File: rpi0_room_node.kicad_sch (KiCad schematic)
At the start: 38 parts, among them J1 Raspberry Pi, J2 Conn_01x03, J3 Conn_01x03, J4 Conn_01x03, Q1 PDTC123Y, U1 AP2210K-3.3, U2 TSOP382xx, U3 RFM69HCW

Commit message: Add ADS1015 ADC
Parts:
- removed AE1: SMA, Connector_Coaxial:SMA_Amphenol_132289_EdgeMount, symbol Device:Antenna_Shield
- removed AE2: U.FL, Connector_Coaxial:U.FL_Hirose_U.FL-R-SMT-1_Vertical, symbol Device:Antenna_Shield
- removed C4: 10u, Capacitor_SMD:C_0805_2012Metric_Pad1.15x1.40mm_HandSolder, symbol Device:C
- removed D1: ASMB-MTB0-0A3A2, LED_SMD:LED_Avago_PLCC4_3.2x2.8mm_CW, symbol LED:ASMB-MTB0-0A3A2
- removed D2: CQY99, LED_THT:LED_D5.0mm_IRGrey, symbol LED:CQY99
- removed D3, D4, D5: LED, LED_SMD:LED_0805_2012Metric_Castellated, symbol Device:LED
- removed J2, J4: Conn_01x03, Connector_PinHeader_2.54mm:PinHeader_1x03_P2.54mm_Vertical, symbol Connector_Generic:Conn_01x03
- removed Q1: PDTC123Y, Package_TO_SOT_SMD:SC-59_Handsoldering, symbol Transistor_BJT:DTA123E
- removed TP5, TP6, TP7: TestPoint, TestPoint:TestPoint_THTPad_1.0x1.0mm_Drill0.5mm, symbol Connector:TestPoint
- removed U1: AP2210K-3.3, Package_TO_SOT_SMD:SOT-23-5, symbol Regulator_Linear:AP2204K-3.3
- removed U2: TSOP382xx, OptoDevice:Vishay_MINICAST-3Pin, symbol Interface_Optical:TSOP382xx
- removed U3: RFM69HCW, RF_Module:HOPERF_RFM69HW, symbol RF_AM_FM:RFM69HCW
- added U1: ADS1015IDGS, Package_SO:TSSOP-10_3x3mm_P0.5mm, symbol Analog_ADC:ADS1015IDGS
- added U2, U3: DS18B20, Connector_PinHeader_2.54mm:PinHeader_1x03_P2.54mm_Vertical, symbol Sensor_Temperature:DS18B20
- C1: value 1u -> 100n; footprint Capacitor_SMD:C_0805_2012Metric_Pad1.15x1.40mm_HandSolder -> Capacitor_SMD:C_0402_1005Metric_Pad0.74x0.62mm_HandSolder
- C2: value 10u -> 100n; footprint Capacitor_SMD:C_0805_2012Metric_Pad1.15x1.40mm_HandSolder -> Capacitor_SMD:C_0402_1005Metric_Pad0.74x0.62mm_HandSolder
- C3: footprint Capacitor_SMD:C_0805_2012Metric_Pad1.15x1.40mm_HandSolder -> Capacitor_SMD:C_0805_2012Metric_Pad1.18x1.45mm_HandSolder
- R1: footprint Resistor_SMD:R_0805_2012Metric_Pad1.15x1.40mm_HandSolder -> Resistor_SMD:R_0402_1005Metric_Pad0.72x0.64mm_HandSolder
- R2: value 70 -> R; footprint Resistor_SMD:R_0805_2012Metric_Pad1.15x1.40mm_HandSolder -> Resistor_SMD:R_0402_1005Metric_Pad0.72x0.64mm_HandSolder
- R3, R4, R5, R6: value 390 -> R; footprint Resistor_SMD:R_0805_2012Metric_Pad1.15x1.40mm_HandSolder -> Resistor_SMD:R_0402_1005Metric_Pad0.72x0.64mm_HandSolder
- R7, R8: value 390 -> 10; footprint Resistor_SMD:R_0805_2012Metric_Pad1.15x1.40mm_HandSolder -> Resistor_SMD:R_0402_1005Metric_Pad0.72x0.64mm_HandSolder
- TP1, TP2, TP3, TP4: footprint TestPoint:TestPoint_THTPad_1.0x1.0mm_Drill0.5mm -> Connector_PinHeader_1.27mm:PinHeader_1x01_P1.27mm_Vertical
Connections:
- net VDDA is gone; now on net +3.3V: C2.1
- net +3.3V: now also J3.3 (Pin_3), R3.2, R5.2, R8.1, U1.8 (VDD)
- net +5V: no longer C1.1
- net GND: now also R4.1, R6.2, U1.3 (GND), U2.1 (GND), U3.1 (GND); no longer J1.14 (Pin_14), J1.20 (Pin_20), J1.25 (Pin_25), J1.30 (Pin_30), J1.34 (Pin_34), J1.39 (Pin_39), J1.9 (Pin_9)
- net ONEWIRE: now also R7.2, U2.2 (DQ), U3.2 (DQ); no longer J1.7 (Pin_7)
- net AI0: now reaches R2.1
- net AI0: now also J3.2 (Pin_2)
- net AIN0: now reaches R2.2
- net AIN0: now also C1.1, R3.1, R4.2, U1.4 (AIN0)
- net 1W_VDD: now reaches R8.2
- net 1W_VDD: now also U2.3 (VDD), U3.3 (VDD)
- net CE0: no longer names the net of J1.24 (Pin_24)
- net IRRX: no longer names the net of J1.12 (Pin_12)
- net IRTX: no longer names the net of J1.11 (Pin_11)
- net LED1 renamed SDA
- net SDA: now also U1.9 (SDA); no longer R3.1
- net LED2 renamed SCL
- net SCL: now also U1.10 (SCL); no longer R4.1
- net LED3: no longer names the net of J1.13 (Pin_13)
- net LED3: no longer R5.1
- net LEDB: no longer names the net of J1.32 (Pin_32)
- net LEDB: no longer R6.1
- net LEDG: no longer names the net of J1.31 (Pin_31)
- net LEDG: no longer R7.1
- net LEDR: no longer names the net of J1.29 (Pin_29)
- net LEDR: no longer R8.1
- net MISO: no longer names the net of J1.21 (Pin_21)
- net MOSI: no longer names the net of J1.19 (Pin_19)
- net RFM_DIO0: no longer names the net of J1.22 (Pin_22)
- net RFM_DIO1: no longer names the net of J1.18 (Pin_18)
- net RFM_DIO2: no longer names the net of J1.16 (Pin_16)
- net RFM_DIO2: no longer TP4.1
- net RFM_DIO3: no longer names the net of TP3.1
- net RFM_DIO3: now also U1.7 (AIN3)
- net RFM_DIO4: no longer names the net of TP2.1
- net RFM_DIO4: now also U1.6 (AIN2)
- net RFM_DIO5: no longer names the net of TP1.1
- net RFM_DIO5: now also U1.5 (AIN1)
- net RFM_RST: no longer names the net of J1.15 (Pin_15)
- net RXD: no longer names the net of J1.10 (Pin_10)
- net RXD: no longer J3.2 (Pin_2)
- net SCLK: no longer names the net of J1.23 (Pin_23)
- net TXD: no longer names the net of J1.8 (Pin_8)
- net TXD: no longer J3.3 (Pin_3)
- new net: J1.7 (Pin_7), R7.1
- new net: R5.1, R6.1, U1.1 (ADDR)
- new net: TP4.1, U1.2 (ALERT/RDY)
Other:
- note removed: "50 mA"
- note removed: "IR receiver"
- note removed: "IR transmitter"
- note removed: "LED indicators"
- note removed: "RF module"
- note removed: "serial port header"
- moved on the sheet: R1

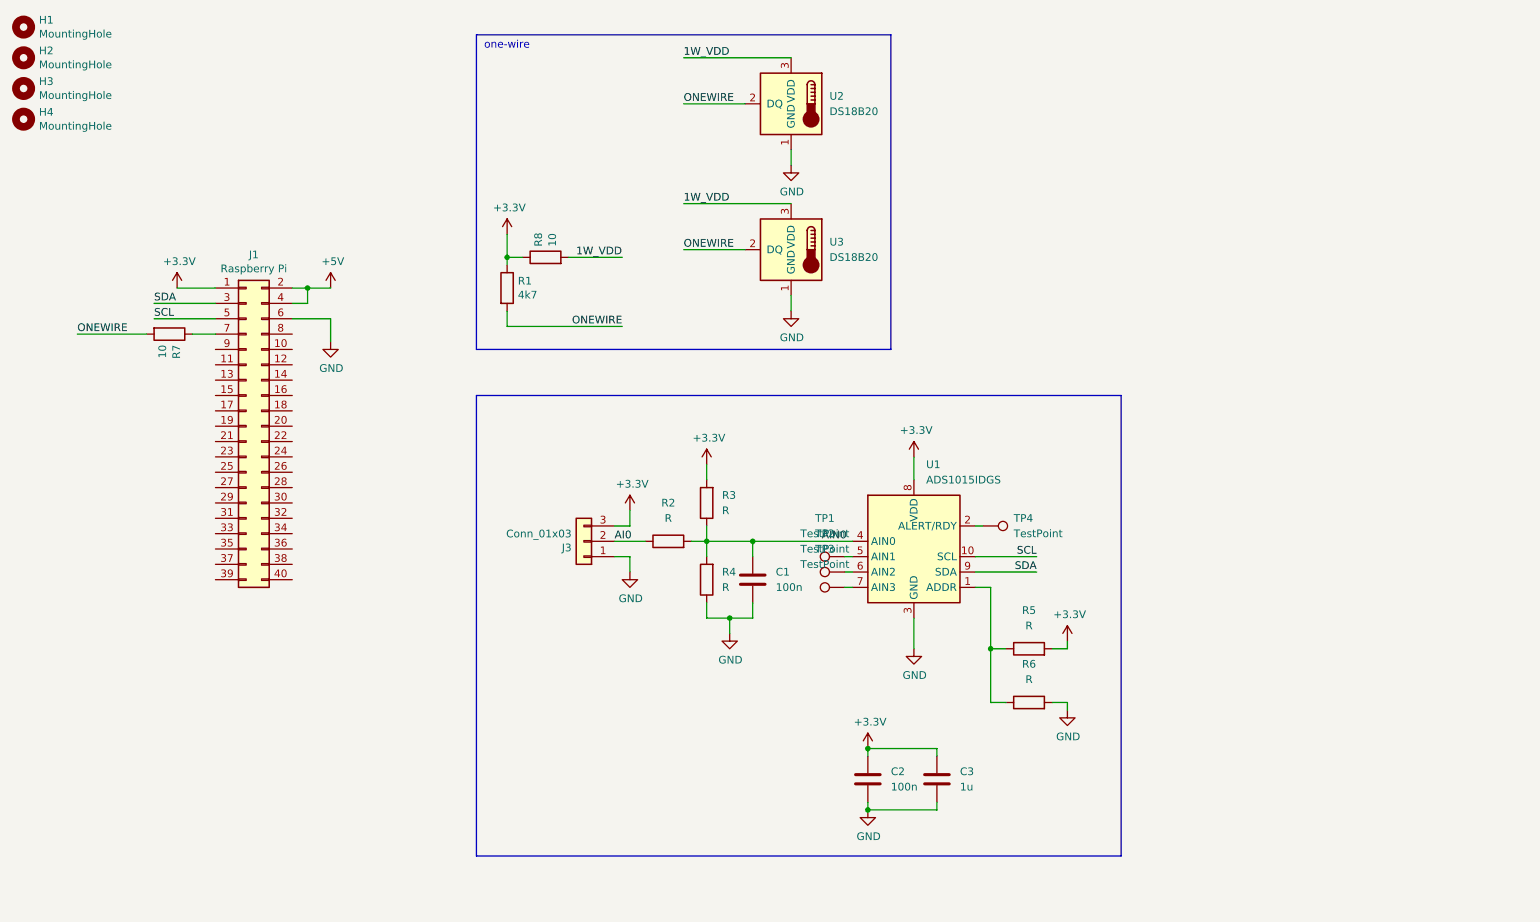
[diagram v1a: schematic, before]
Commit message: Add one-wire chip
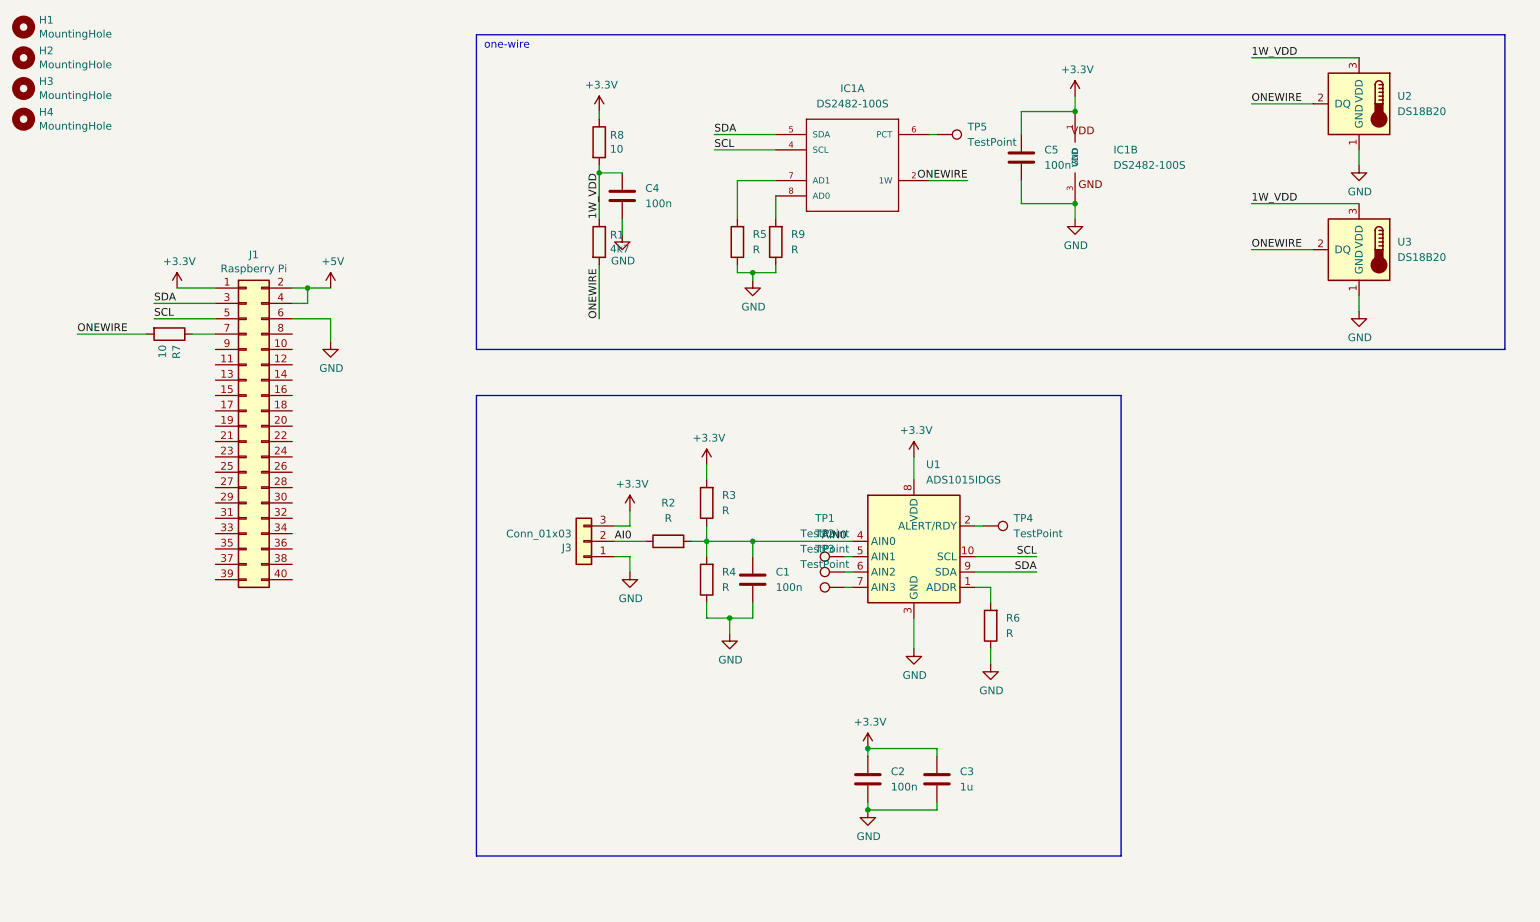
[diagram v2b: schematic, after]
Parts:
- added C4, C5: 100n, Capacitor_SMD:C_0402_1005Metric_Pad0.74x0.62mm_HandSolder, symbol Device:C
- added IC1: DS2482-100S, Package_SO:SO-8_3.9x4.9mm_P1.27mm, symbol 1wire:DS2482-100S
- added R9: R, NetTie:NetTie-2_THT_Pad0.3mm, symbol Device:R
- added TP5: TestPoint, Connector_PinHeader_1.27mm:PinHeader_1x01_P1.27mm_Vertical, symbol Connector:TestPoint
- J3, U2, U3: footprint Connector_PinHeader_2.54mm:PinHeader_1x03_P2.54mm_Vertical -> Connector_JST:JST_PH_B3B-PH-SM4-TB_1x03-1MP_P2.00mm_Vertical
- R5, R6: footprint Resistor_SMD:R_0402_1005Metric_Pad0.72x0.64mm_HandSolder -> NetTie:NetTie-2_THT_Pad0.3mm
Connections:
- net +3.3V: now also C5.2, IC1.1 (VDD); no longer R1.1, R5.2
- net 1W_VDD: now also R1.1, C4.2
- net GND: now also R5.1, R6.1, C4.1, C5.1, IC1.3 (GND), R9.1; no longer R6.2
- net ONEWIRE: now also IC1.2 (1W)
- net SCL: now also IC1.4 (SCL)
- net SDA: now also IC1.5 (SDA)
- new net: R6.2, U1.1 (ADDR)
- new net: IC1.7 (AD1), R5.2
- new net: IC1.8 (AD0), R9.2
- new net: IC1.6 (PCT), TP5.1
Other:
- moved on the sheet: R1, R6, R8, U2, U3

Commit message: Polishing
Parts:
- removed TP1: TestPoint, Connector_PinHeader_1.27mm:PinHeader_1x01_P1.27mm_Vertical, symbol Connector:TestPoint
- added C6: 100n, Capacitor_SMD:C_0603_1608Metric_Pad1.08x0.95mm_HandSolder, symbol Device:C
- added J2: Conn_01x03, Connector_JST:JST_PH_B3B-PH-SM4-TB_1x03-1MP_P2.00mm_Vertical, symbol Connector_Generic:Conn_01x03
- added R10, R11, R12: R, Resistor_SMD:R_0603_1608Metric_Pad0.98x0.95mm_HandSolder, symbol Device:R
- C1: footprint Capacitor_SMD:C_0402_1005Metric_Pad0.74x0.62mm_HandSolder -> Capacitor_SMD:C_0603_1608Metric_Pad1.08x0.95mm_HandSolder
- C3: value 1u -> DNP
- R2, R3, R4: footprint Resistor_SMD:R_0402_1005Metric_Pad0.72x0.64mm_HandSolder -> Resistor_SMD:R_0603_1608Metric_Pad0.98x0.95mm_HandSolder
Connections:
- net +3.3V: now also J2.3 (Pin_3), R11.2
- net GND: now also J1.14 (Pin_14), J1.20 (Pin_20), J1.25 (Pin_25), J1.30 (Pin_30), J1.34 (Pin_34), J1.39 (Pin_39), J1.9 (Pin_9), C6.2, J2.1 (Pin_1), R12.1
- net AIN1: now reaches U1.5 (AIN1)
- net AIN1: now also C6.1, R10.2, R11.1, R12.2
- new net AI1: J2.2 (Pin_2), R10.1
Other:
- moved on the sheet: C1, C2, C3, J3, R2, R3, R4

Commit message: Add 2.54 mm holes to JST connectors
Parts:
- J2, J3, U2, U3: footprint Connector_JST:JST_PH_B3B-PH-SM4-TB_1x03-1MP_P2.00mm_Vertical -> weird connectors:JST_PH_B3B-PH-SM4-TB_1x03-1MP_P2.00mm_Vertical + 2.54 mm header
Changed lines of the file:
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@@
       (effects (font (size 1.27 1.27)) (justify right))
     )
-    (property "Footprint" "Connector_JST:JST_PH_B3B-PH-SM4-TB_1x03-1MP_P2.00mm_Vertical" (id 2) (at 266.7 40.64 0)
+    (property "Footprint" "weird connectors:JST_PH_B3B-PH-SM4-TB_1x03-1MP_P2.00mm_Vertical + 2.54 mm header" (id 2) (at 266.7 40.64 0)
       (effects (font (size 1.27 1.27)) hide)
     )
@@
       (effects (font (size 1.27 1.27)) (justify left))
     )
-    (property "Footprint" "Connector_JST:JST_PH_B3B-PH-SM4-TB_1x03-1MP_P2.00mm_Vertical" (id 2) (at 116.84 146.05 0)
+    (property "Footprint" "weird connectors:JST_PH_B3B-PH-SM4-TB_1x03-1MP_P2.00mm_Vertical + 2.54 mm header" (id 2) (at 116.84 146.05 0)
       (effects (font (size 1.27 1.27)) hide)
     )
@@
       (effects (font (size 1.27 1.27)) (justify right))
     )
-    (property "Footprint" "Connector_JST:JST_PH_B3B-PH-SM4-TB_1x03-1MP_P2.00mm_Vertical" (id 2) (at 266.7 64.77 0)
+    (property "Footprint" "weird connectors:JST_PH_B3B-PH-SM4-TB_1x03-1MP_P2.00mm_Vertical + 2.54 mm header" (id 2) (at 266.7 64.77 0)
       (effects (font (size 1.27 1.27)) hide)
     )
@@
       (effects (font (size 1.27 1.27)) (justify left))
     )
-    (property "Footprint" "Connector_JST:JST_PH_B3B-PH-SM4-TB_1x03-1MP_P2.00mm_Vertical" (id 2) (at 113.03 102.87 0)
+    (property "Footprint" "weird connectors:JST_PH_B3B-PH-SM4-TB_1x03-1MP_P2.00mm_Vertical + 2.54 mm header" (id 2) (at 113.03 102.87 0)
       (effects (font (size 1.27 1.27)) hide)
     )
@@
     )
     (path "/bf873bad-260d-42de-b5d4-cb40eef6de8a"
-      (reference "J2") (unit 1) (value "Conn_01x03") (footprint "Connector_JST:JST_PH_B3B-PH-SM4-TB_1x03-1MP_P2.00mm_Vertical")
+      (reference "J2") (unit 1) (value "Conn_01x03") (footprint "weird connectors:JST_PH_B3B-PH-SM4-TB_1x03-1MP_P2.00mm_Vertical + 2.54 mm header")
     )
     (path "/ffdc1f33-4246-483a-8c26-8acd0a26a711"
-      (reference "J3") (unit 1) (value "Conn_01x03") (footprint "Connector_JST:JST_PH_B3B-PH-SM4-TB_1x03-1MP_P2.00mm_Vertical")
+      (reference "J3") (unit 1) (value "Conn_01x03") (footprint "weird connectors:JST_PH_B3B-PH-SM4-TB_1x03-1MP_P2.00mm_Vertical + 2.54 mm header")
     )
     (path "/00000000-0000-0000-0000-00005c2cf51b"
@@
     )
     (path "/696ddb21-627f-41c6-ae12-3a6fbdfba463"
-      (reference "U2") (unit 1) (value "DS18B20") (footprint "Connector_JST:JST_PH_B3B-PH-SM4-TB_1x03-1MP_P2.00mm_Vertical")
+      (reference "U2") (unit 1) (value "DS18B20") (footprint "weird connectors:JST_PH_B3B-PH-SM4-TB_1x03-1MP_P2.00mm_Vertical + 2.54 mm header")
     )
     (path "/ee756404-333d-4120-ad21-da61557face2"
-      (reference "U3") (unit 1) (value "DS18B20") (footprint "Connector_JST:JST_PH_B3B-PH-SM4-TB_1x03-1MP_P2.00mm_Vertical")
-    )
-  )
+      (reference "U3") (unit 1) (value "DS18B20") (footprint "weird connectors:JST_PH_B3B-PH-SM4-TB_1x03-1MP_P2.00mm_Vertical + 2.54 mm header")
+    )
+  )
